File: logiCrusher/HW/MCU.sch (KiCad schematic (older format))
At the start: 16 parts

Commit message: Added the front plate files
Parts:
- removed RV? (x4): R_POT_US, symbol Device:R_POT_US
- removed TP?: TestPoint, symbol Connector:TestPoint
- added R? (x2): 0R, Resistor_SMD:R_0805_2012Metric, symbol Device:R_US
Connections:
- net labels added: Vin, Vout
- net labels removed: TRIG
- wire segments 113 -> 103
- no-connect marks 1 -> 0
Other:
- note added: "Has this been checked?"
- note removed: "K1"
- note removed: "K2"
- note removed: "K3"
- note removed: "K4"
- moved on the sheet: C?, J?, SW?

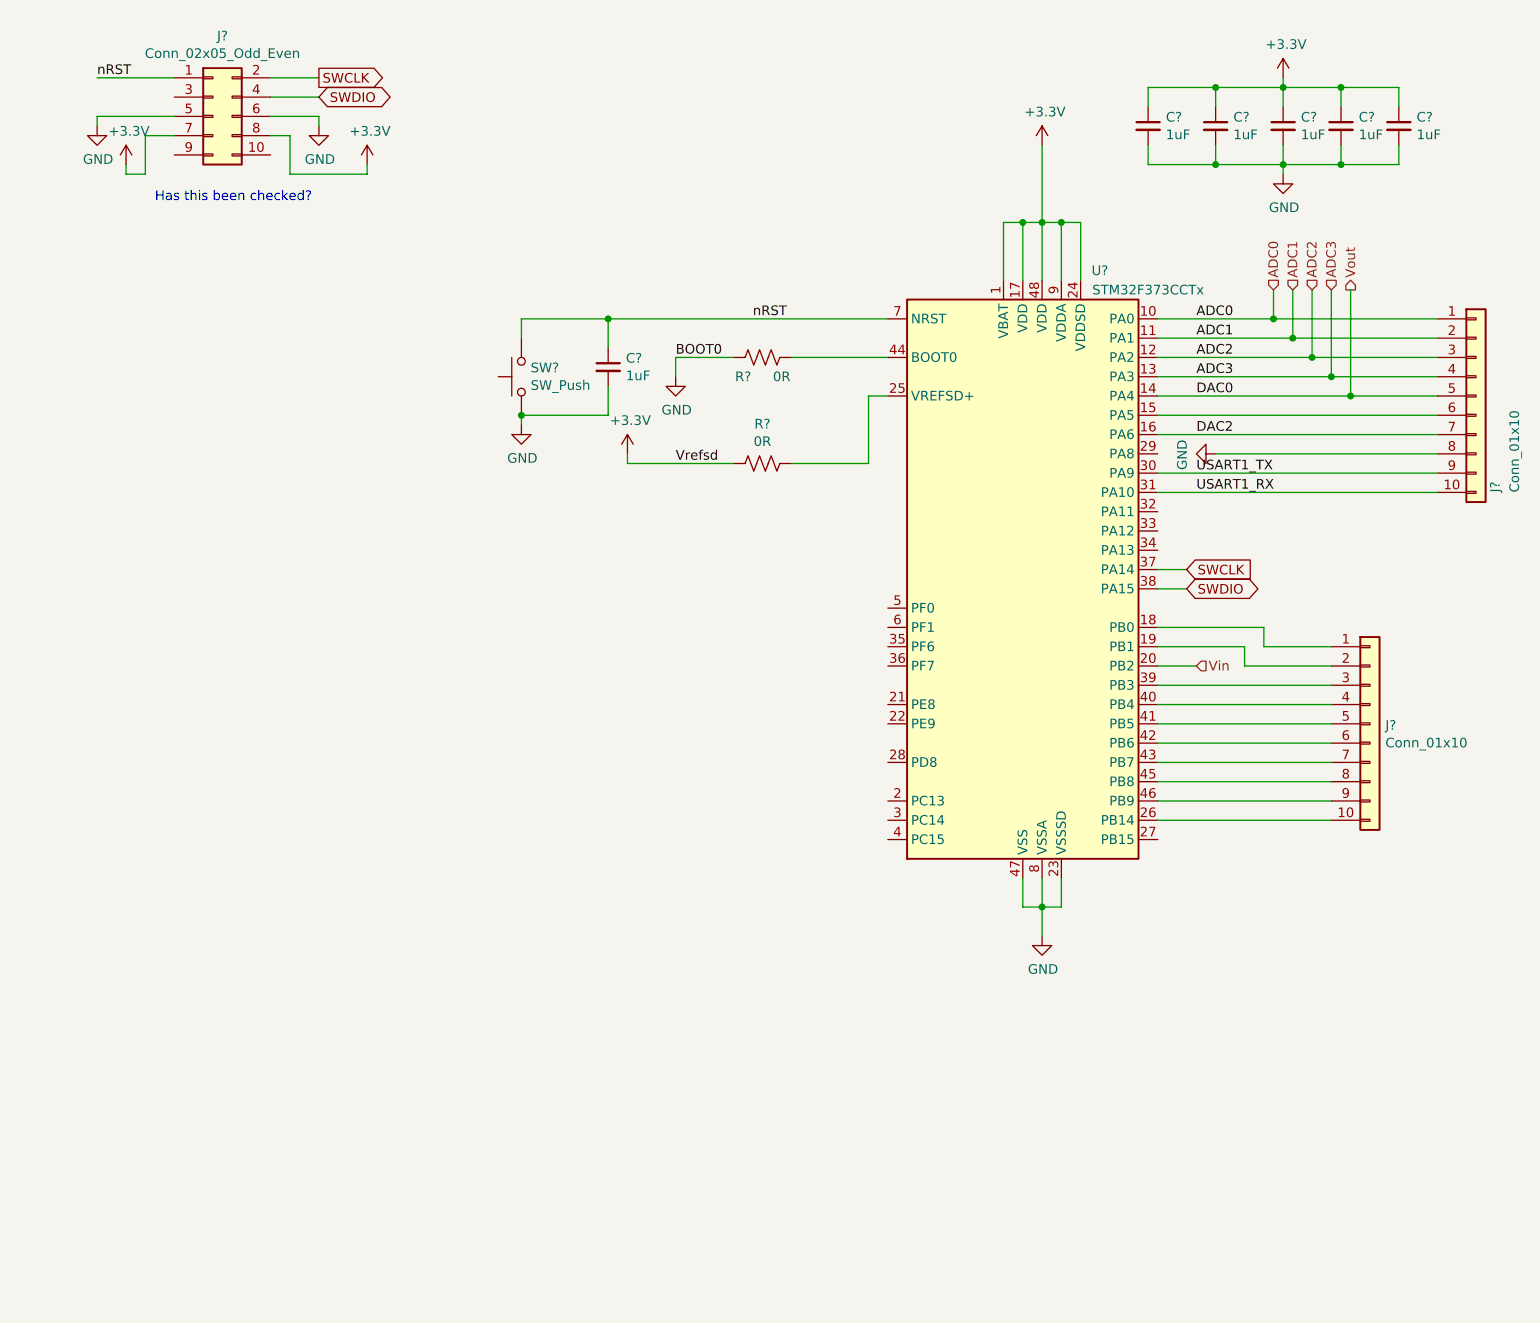
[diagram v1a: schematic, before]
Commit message: Worked on the HW for the mcu module
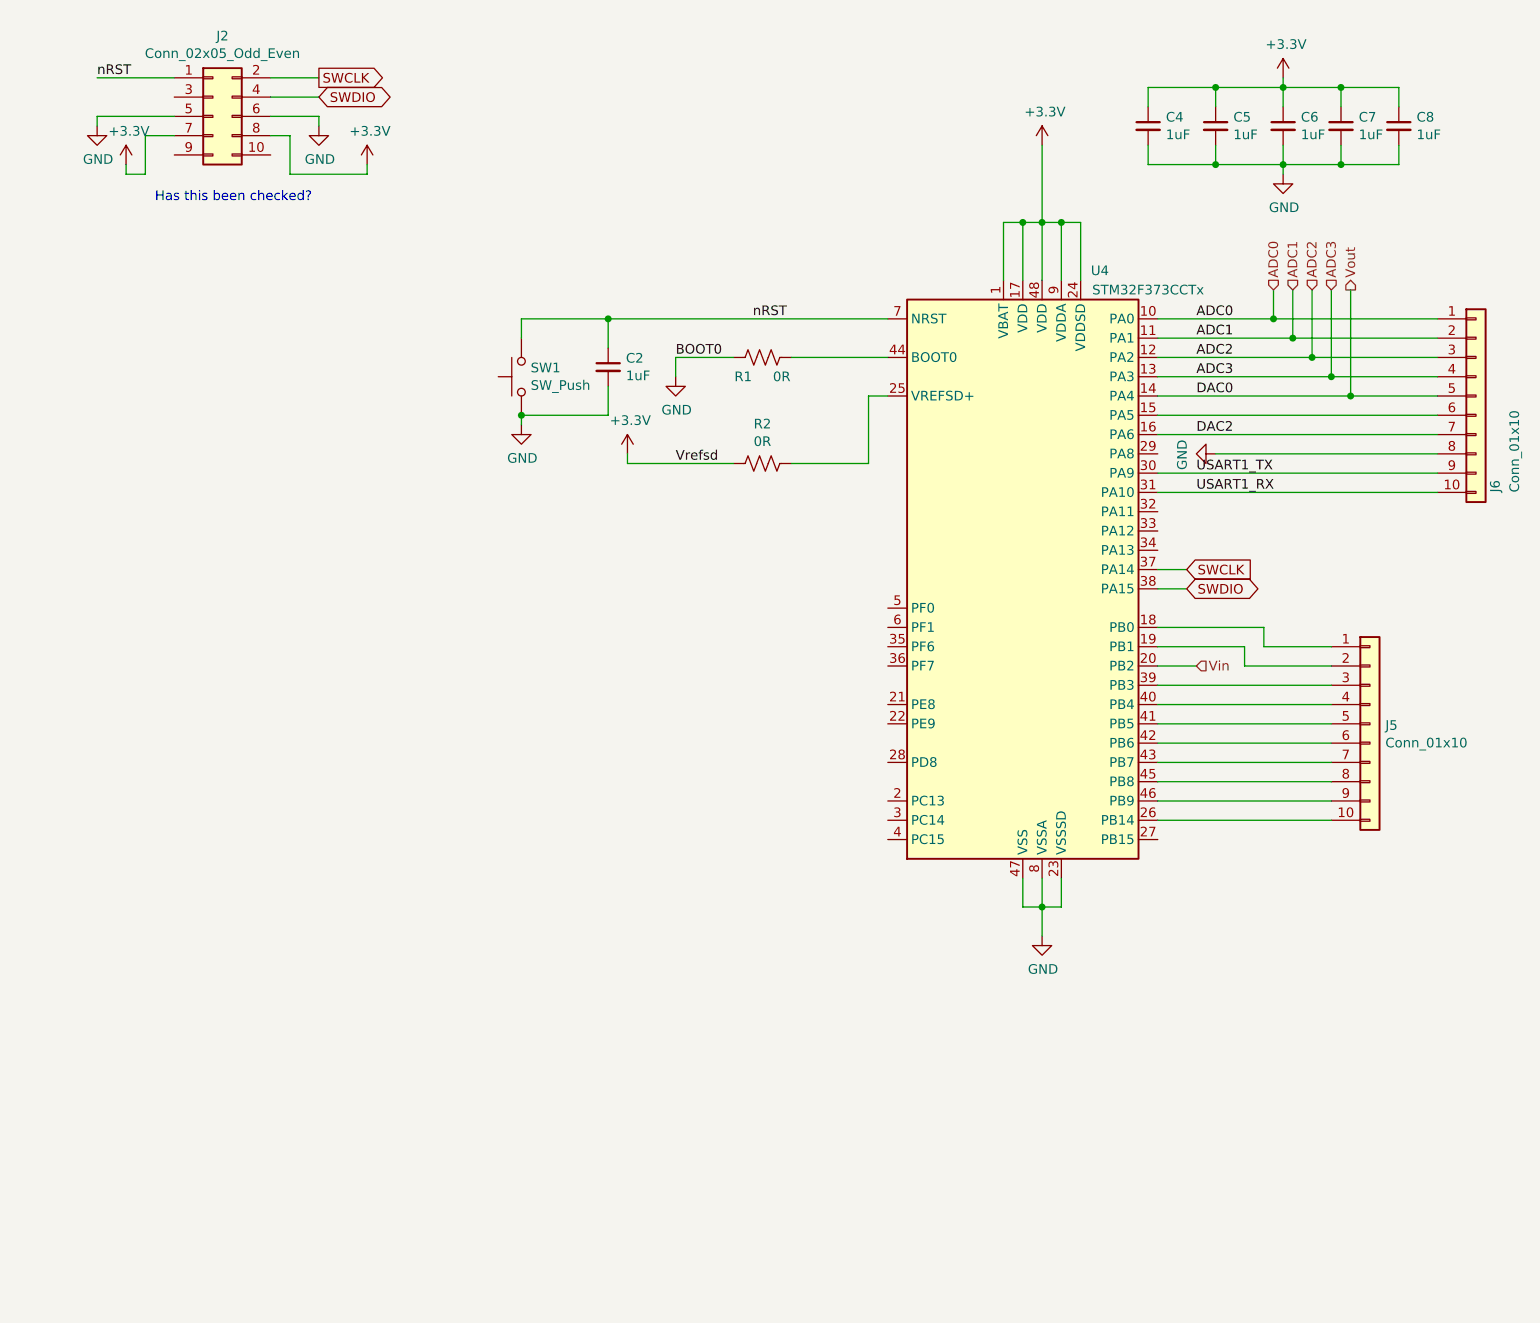
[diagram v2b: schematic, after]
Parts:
- gave numbers to parts that had none: 13
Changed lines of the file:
@@
 P 5950 3850
 AR Path="/5CB1AF0D" Ref="U?"  Part="1"
-AR Path="/5CB08311/5CB1AF0D" Ref="U?"  Part="1"
-F 0 "U?" H 6350 5400 50  0000 C CNN
+AR Path="/5CB08311/5CB1AF0D" Ref="U4"  Part="1"
+F 0 "U4" H 6350 5400 50  0000 C CNN
 F 1 "STM32F373CCTx" H 6600 5300 50  0000 C CNN
 F 2 "Package_QFP:LQFP-48_7x7mm_P0.5mm" H 5350 2350 50  0001 R CNN
@@
 P 6050 1650
 AR Path="/5CB1AF30" Ref="#PWR?"  Part="1"
-AR Path="/5CB08311/5CB1AF30" Ref="#PWR?"  Part="1"
-F 0 "#PWR?" H 6050 1500 50  0001 C CNN
+AR Path="/5CB08311/5CB1AF30" Ref="#PWR027"  Part="1"
+F 0 "#PWR027" H 6050 1500 50  0001 C CNN
 F 1 "+3.3V" H 6065 1823 50  0000 C CNN
 F 2 "" H 6050 1650 50  0001 C CNN
@@
 P 6050 5750
 AR Path="/5CB1AF3C" Ref="#PWR?"  Part="1"
-AR Path="/5CB08311/5CB1AF3C" Ref="#PWR?"  Part="1"
-F 0 "#PWR?" H 6050 5500 50  0001 C CNN
+AR Path="/5CB08311/5CB1AF3C" Ref="#PWR028"  Part="1"
+F 0 "#PWR028" H 6050 5500 50  0001 C CNN
 F 1 "GND" H 6055 5577 50  0000 C CNN
 F 2 "" H 6050 5750 50  0001 C CNN
@@
 P 6600 1550
 AR Path="/5CB1AF47" Ref="C?"  Part="1"
-AR Path="/5CB08311/5CB1AF47" Ref="C?"  Part="1"
-F 0 "C?" H 6692 1596 50  0000 L CNN
+AR Path="/5CB08311/5CB1AF47" Ref="C4"  Part="1"
+F 0 "C4" H 6692 1596 50  0000 L CNN
 F 1 "1uF" H 6692 1505 50  0000 L CNN
 F 2 "Capacitor_SMD:C_0805_2012Metric" H 6600 1550 50  0001 C CNN
@@
 P 6950 1550
 AR Path="/5CB1AF4E" Ref="C?"  Part="1"
-AR Path="/5CB08311/5CB1AF4E" Ref="C?"  Part="1"
-F 0 "C?" H 7042 1596 50  0000 L CNN
+AR Path="/5CB08311/5CB1AF4E" Ref="C5"  Part="1"
+F 0 "C5" H 7042 1596 50  0000 L CNN
 F 1 "1uF" H 7042 1505 50  0000 L CNN
 F 2 "Capacitor_SMD:C_0805_2012Metric" H 6950 1550 50  0001 C CNN
@@
 P 7300 1550
 AR Path="/5CB1AF55" Ref="C?"  Part="1"
-AR Path="/5CB08311/5CB1AF55" Ref="C?"  Part="1"
-F 0 "C?" H 7392 1596 50  0000 L CNN
+AR Path="/5CB08311/5CB1AF55" Ref="C6"  Part="1"
+F 0 "C6" H 7392 1596 50  0000 L CNN
 F 1 "1uF" H 7392 1505 50  0000 L CNN
 F 2 "Capacitor_SMD:C_0805_2012Metric" H 7300 1550 50  0001 C CNN
@@
 P 7600 1550
 AR Path="/5CB1AF5C" Ref="C?"  Part="1"
-AR Path="/5CB08311/5CB1AF5C" Ref="C?"  Part="1"
-F 0 "C?" H 7692 1596 50  0000 L CNN
+AR Path="/5CB08311/5CB1AF5C" Ref="C7"  Part="1"
+F 0 "C7" H 7692 1596 50  0000 L CNN
 F 1 "1uF" H 7692 1505 50  0000 L CNN
 F 2 "Capacitor_SMD:C_0805_2012Metric" H 7600 1550 50  0001 C CNN
@@
 P 7900 1550
 AR Path="/5CB1AF63" Ref="C?"  Part="1"
-AR Path="/5CB08311/5CB1AF63" Ref="C?"  Part="1"
-F 0 "C?" H 7992 1596 50  0000 L CNN
+AR Path="/5CB08311/5CB1AF63" Ref="C8"  Part="1"
+F 0 "C8" H 7992 1596 50  0000 L CNN
 F 1 "1uF" H 7992 1505 50  0000 L CNN
 F 2 "Capacitor_SMD:C_0805_2012Metric" H 7900 1550 50  0001 C CNN
@@
 P 7300 1300
 AR Path="/5CB1AF6B" Ref="#PWR?"  Part="1"
-AR Path="/5CB08311/5CB1AF6B" Ref="#PWR?"  Part="1"
-F 0 "#PWR?" H 7300 1150 50  0001 C CNN
+AR Path="/5CB08311/5CB1AF6B" Ref="#PWR030"  Part="1"
+F 0 "#PWR030" H 7300 1150 50  0001 C CNN
 F 1 "+3.3V" H 7315 1473 50  0000 C CNN
 F 2 "" H 7300 1300 50  0001 C CNN
@@
 P 7300 1800
 AR Path="/5CB1AF71" Ref="#PWR?"  Part="1"
-AR Path="/5CB08311/5CB1AF71" Ref="#PWR?"  Part="1"
-F 0 "#PWR?" H 7300 1550 50  0001 C CNN
+AR Path="/5CB08311/5CB1AF71" Ref="#PWR031"  Part="1"
+F 0 "#PWR031" H 7300 1550 50  0001 C CNN
 F 1 "GND" H 7305 1627 50  0000 C CNN
 F 2 "" H 7300 1800 50  0001 C CNN
@@
 P 3350 2850
 AR Path="/5CB1AF99" Ref="SW?"  Part="1"
-AR Path="/5CB08311/5CB1AF99" Ref="SW?"  Part="1"
-F 0 "SW?" V 3396 2802 50  0000 R CNN
+AR Path="/5CB08311/5CB1AF99" Ref="SW1"  Part="1"
+F 0 "SW1" V 3396 2802 50  0000 R CNN
 F 1 "SW_Push" V 3305 2802 50  0000 R CNN
 F 2 "" H 3350 3050 50  0001 C CNN
@@
 P 3350 3100
 AR Path="/5CB1AFA3" Ref="#PWR?"  Part="1"
-AR Path="/5CB08311/5CB1AFA3" Ref="#PWR?"  Part="1"
-F 0 "#PWR?" H 3350 2850 50  0001 C CNN
+AR Path="/5CB08311/5CB1AFA3" Ref="#PWR024"  Part="1"
+F 0 "#PWR024" H 3350 2850 50  0001 C CNN
 F 1 "GND" H 3355 2927 50  0000 C CNN
 F 2 "" H 3350 3100 50  0001 C CNN
@@
 P 3800 2800
 AR Path="/5CB1AFA9" Ref="C?"  Part="1"
-AR Path="/5CB08311/5CB1AFA9" Ref="C?"  Part="1"
-F 0 "C?" H 3892 2846 50  0000 L CNN
+AR Path="/5CB08311/5CB1AFA9" Ref="C2"  Part="1"
+F 0 "C2" H 3892 2846 50  0000 L CNN
 F 1 "1uF" H 3892 2755 50  0000 L CNN
 F 2 "Capacitor_SMD:C_0805_2012Metric" H 3800 2800 50  0001 C CNN
@@
 P 7750 4650
 AR Path="/5CB1AFBC" Ref="J?"  Part="1"
-AR Path="/5CB08311/5CB1AFBC" Ref="J?"  Part="1"
-F 0 "J?" H 7830 4642 50  0000 L CNN
+AR Path="/5CB08311/5CB1AFBC" Ref="J5"  Part="1"
+F 0 "J5" H 7830 4642 50  0000 L CNN
 F 1 "Conn_01x10" H 7830 4551 50  0000 L CNN
 F 2 "" H 7750 4650 50  0001 C CNN
@@
 P 8300 2950
 AR Path="/5CB1AFEA" Ref="J?"  Part="1"
-AR Path="/5CB08311/5CB1AFEA" Ref="J?"  Part="1"
-F 0 "J?" V 8400 2450 50  0000 L CNN
+AR Path="/5CB08311/5CB1AFEA" Ref="J6"  Part="1"
+F 0 "J6" V 8400 2450 50  0000 L CNN
 F 1 "Conn_01x10" V 8500 2450 50  0000 L CNN
 F 2 "" H 8300 2950 50  0001 C CNN
@@
 P 6950 3250
 AR Path="/5CB1B004" Ref="#PWR?"  Part="1"
-AR Path="/5CB08311/5CB1B004" Ref="#PWR?"  Part="1"
-F 0 "#PWR?" H 6950 3000 50  0001 C CNN
+AR Path="/5CB08311/5CB1B004" Ref="#PWR029"  Part="1"
+F 0 "#PWR029" H 6950 3000 50  0001 C CNN
 F 1 "GND" H 6955 3077 50  0000 C CNN
 F 2 "" H 6950 3250 50  0001 C CNN
@@
 P 1750 1500
 AR Path="/5CBA4E93" Ref="J?"  Part="1"
-AR Path="/5CB08311/5CBA4E93" Ref="J?"  Part="1"
-F 0 "J?" H 1800 1917 50  0000 C CNN
+AR Path="/5CB08311/5CBA4E93" Ref="J2"  Part="1"
+F 0 "J2" H 1800 1917 50  0000 C CNN
 F 1 "Conn_02x05_Odd_Even" H 1800 1826 50  0000 C CNN
 F 2 "" H 1750 1500 50  0001 C CNN
@@
 P 1150 1550
 AR Path="/5CBA4E9D" Ref="#PWR?"  Part="1"
-AR Path="/5CB08311/5CBA4E9D" Ref="#PWR?"  Part="1"
-F 0 "#PWR?" H 1150 1300 50  0001 C CNN
+AR Path="/5CB08311/5CBA4E9D" Ref="#PWR019"  Part="1"
+F 0 "#PWR019" H 1150 1300 50  0001 C CNN
 F 1 "GND" H 1155 1377 50  0000 C CNN
 F 2 "" H 1150 1550 50  0001 C CNN
@@
 P 2300 1550
 AR Path="/5CBA4EA3" Ref="#PWR?"  Part="1"
-AR Path="/5CB08311/5CBA4EA3" Ref="#PWR?"  Part="1"
-F 0 "#PWR?" H 2300 1300 50  0001 C CNN
+AR Path="/5CB08311/5CBA4EA3" Ref="#PWR022"  Part="1"
+F 0 "#PWR022" H 2300 1300 50  0001 C CNN
 F 1 "GND" H 2305 1377 50  0000 C CNN
 F 2 "" H 2300 1550 50  0001 C CNN
@@
 P 1300 1750
 AR Path="/5CBA4EAD" Ref="#PWR?"  Part="1"
-AR Path="/5CB08311/5CBA4EAD" Ref="#PWR?"  Part="1"
-F 0 "#PWR?" H 1300 1600 50  0001 C CNN
+AR Path="/5CB08311/5CBA4EAD" Ref="#PWR021"  Part="1"
+F 0 "#PWR021" H 1300 1600 50  0001 C CNN
 F 1 "+3.3V" H 1315 1923 50  0000 C CNN
 F 2 "" H 1300 1750 50  0001 C CNN
@@
 P 2550 1750
 AR Path="/5CBA4EBB" Ref="#PWR?"  Part="1"
-AR Path="/5CB08311/5CBA4EBB" Ref="#PWR?"  Part="1"
-F 0 "#PWR?" H 2550 1600 50  0001 C CNN
+AR Path="/5CB08311/5CBA4EBB" Ref="#PWR023"  Part="1"
+F 0 "#PWR023" H 2550 1600 50  0001 C CNN
 F 1 "+3.3V" H 2565 1923 50  0000 C CNN
 F 2 "" H 2550 1750 50  0001 C CNN
@@
 P 4600 3300
 AR Path="/5CB92368/5CBF628D" Ref="R?"  Part="1"
-AR Path="/5CB08311/5CBF628D" Ref="R?"  Part="1"
-F 0 "R?" V 4395 3300 50  0000 C CNN
+AR Path="/5CB08311/5CBF628D" Ref="R2"  Part="1"
+F 0 "R2" V 4395 3300 50  0000 C CNN
 F 1 "0R" V 4486 3300 50  0000 C CNN
 F 2 "Resistor_SMD:R_0805_2012Metric" V 4640 3290 50  0001 C CNN
@@
 P 4600 2750
 AR Path="/5CB92368/5CC048C6" Ref="R?"  Part="1"
-AR Path="/5CB08311/5CC048C6" Ref="R?"  Part="1"
-F 0 "R?" V 4700 2650 50  0000 C CNN
+AR Path="/5CB08311/5CC048C6" Ref="R1"  Part="1"
+F 0 "R1" V 4700 2650 50  0000 C CNN
 F 1 "0R" V 4700 2850 50  0000 C CNN
 F 2 "Resistor_SMD:R_0805_2012Metric" V 4640 2740 50  0001 C CNN
@@
 P 4150 2850
 AR Path="/5CC0916A" Ref="#PWR?"  Part="1"
-AR Path="/5CB08311/5CC0916A" Ref="#PWR?"  Part="1"
-F 0 "#PWR?" H 4150 2600 50  0001 C CNN
+AR Path="/5CB08311/5CC0916A" Ref="#PWR026"  Part="1"
+F 0 "#PWR026" H 4150 2600 50  0001 C CNN
 F 1 "GND" H 4155 2677 50  0000 C CNN
 F 2 "" H 4150 2850 50  0001 C CNN
@@
 P 3900 3250
 AR Path="/5CC316EF" Ref="#PWR?"  Part="1"
-AR Path="/5CB08311/5CC316EF" Ref="#PWR?"  Part="1"
-F 0 "#PWR?" H 3900 3100 50  0001 C CNN
+AR Path="/5CB08311/5CC316EF" Ref="#PWR025"  Part="1"
+F 0 "#PWR025" H 3900 3100 50  0001 C CNN
 F 1 "+3.3V" H 3915 3423 50  0000 C CNN
 F 2 "" H 3900 3250 50  0001 C CNN
